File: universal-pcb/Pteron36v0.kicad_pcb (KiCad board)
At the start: 2 copper layers, 140.1 x 108.1 mm, 62 parts, among them J1 AudioJack4, J2 AudioJack4, J3 Conn_01x04, SW10 SW_PUSH, SW12 SW_PUSH, SW13 SW_PUSH, SW14 SW_PUSH, SW15 SW_PUSH, SW17 SW_PUSH, SW18 SW_PUSH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

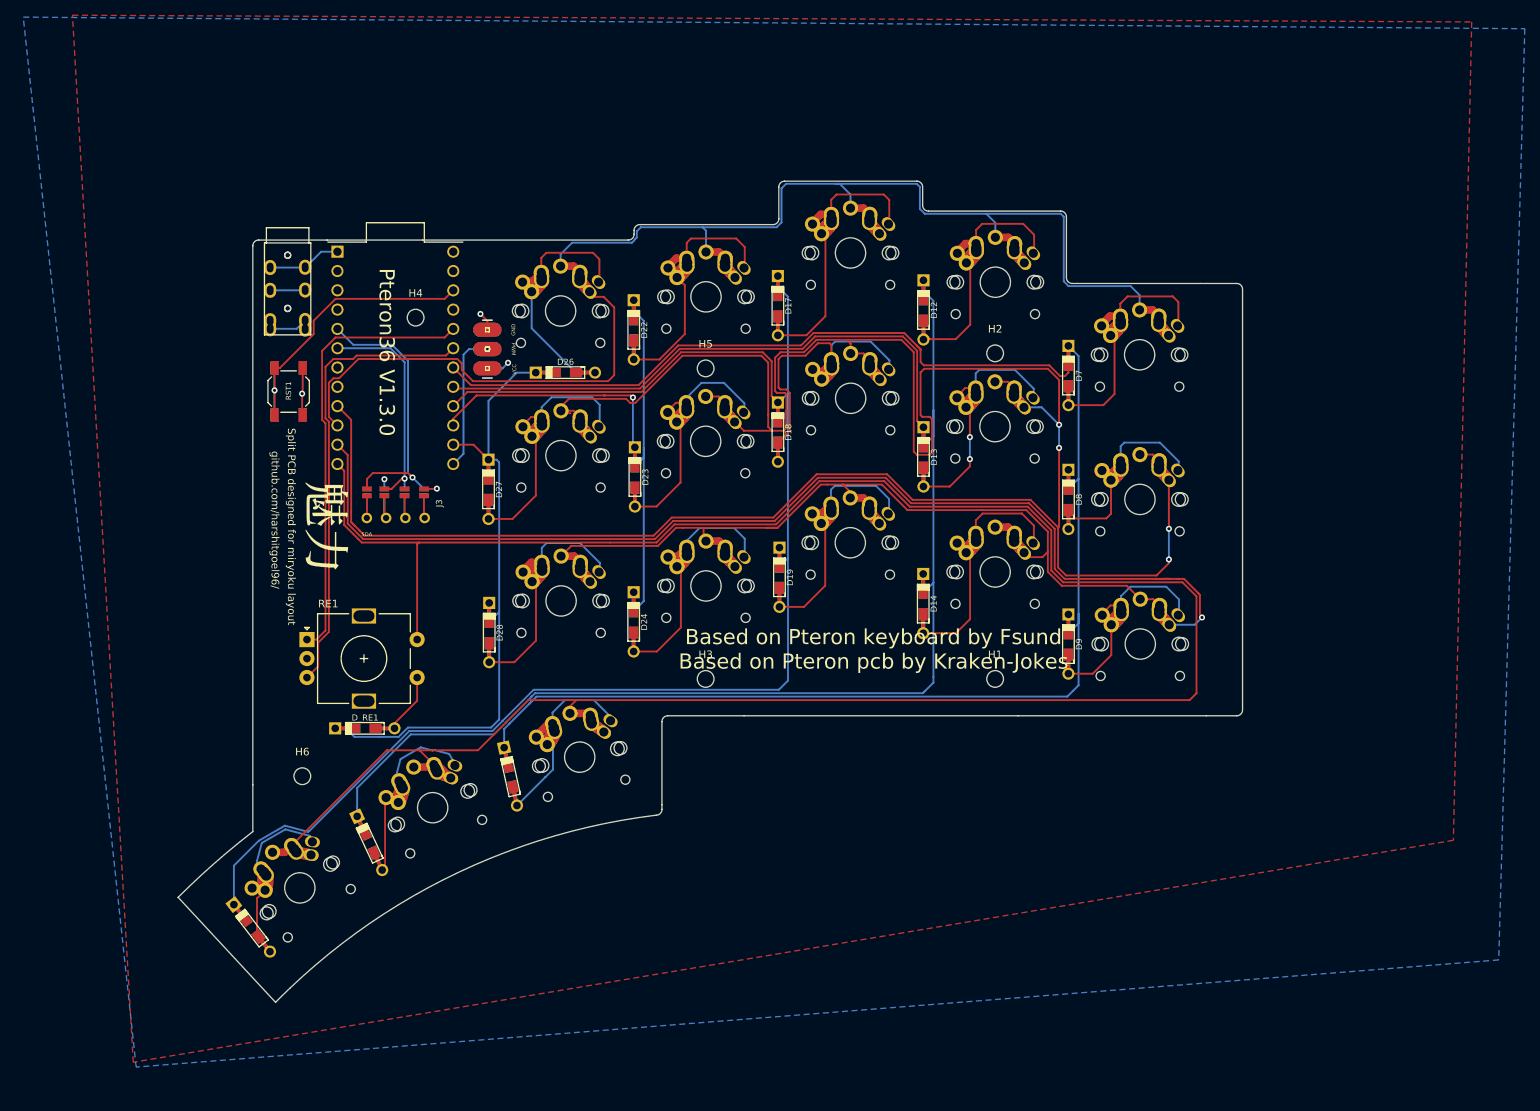
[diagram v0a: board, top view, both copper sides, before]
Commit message: update universal pcb with curvy layout
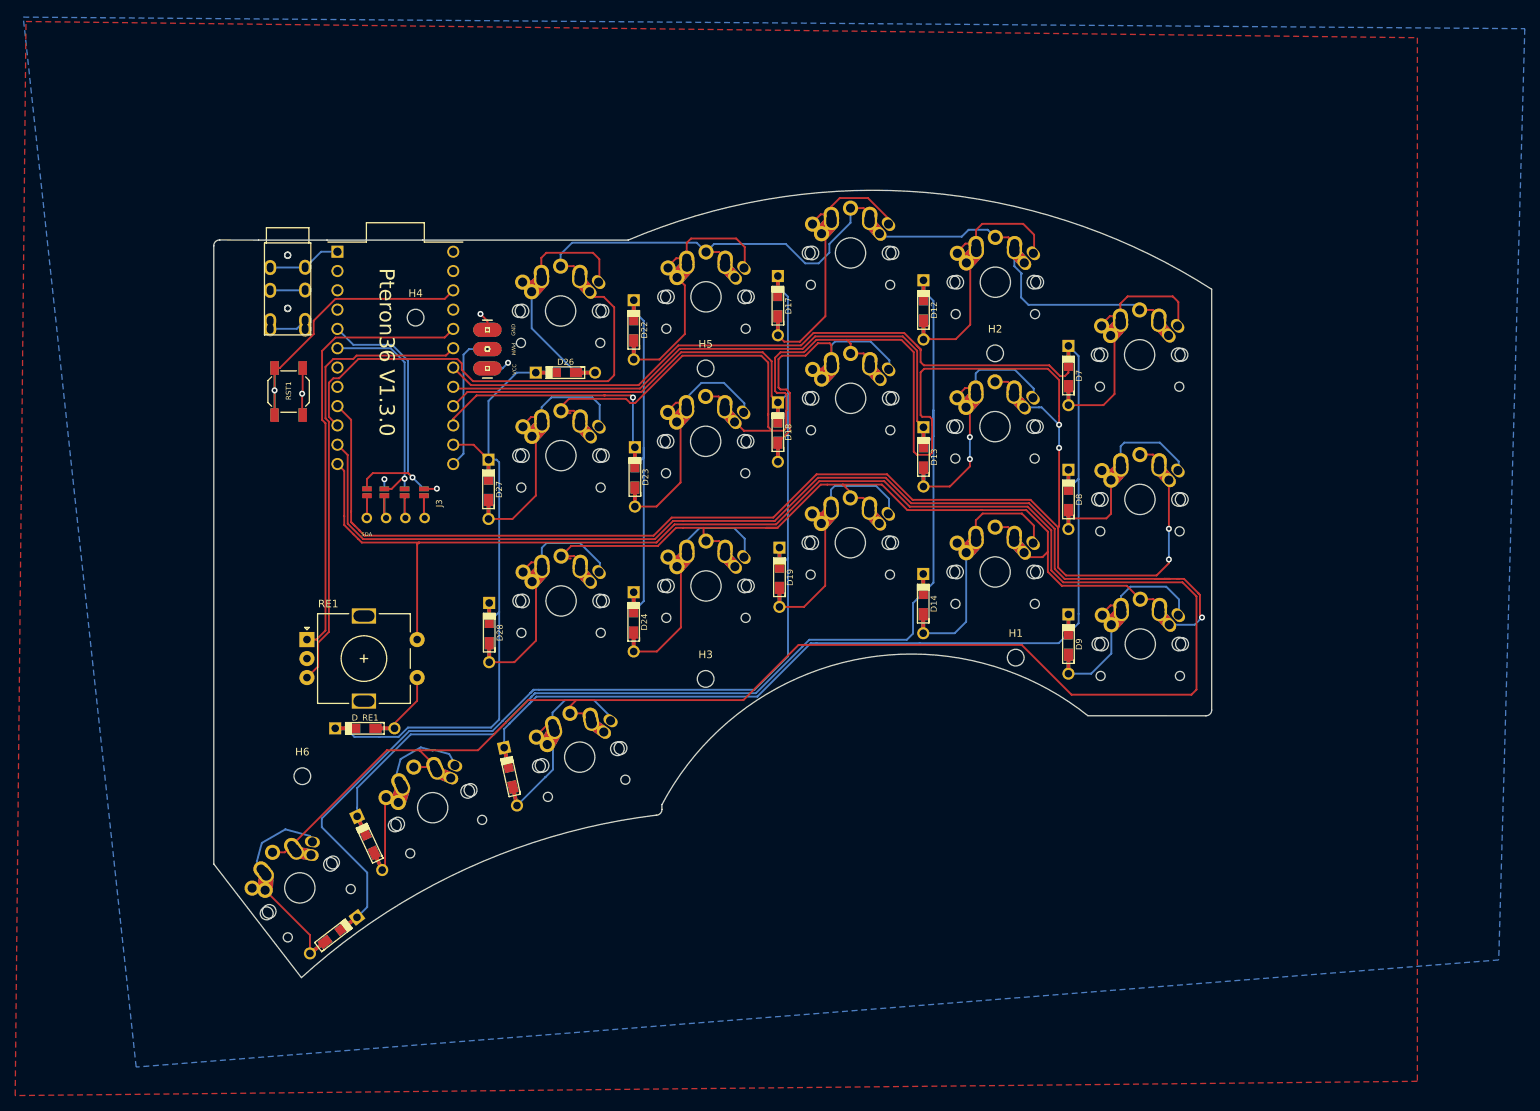
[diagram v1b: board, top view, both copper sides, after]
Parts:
- removed LOGO1, LOGO2: LOGO-OTL, personal-logo:miryoku-kicad-small
- moved D20 10.8 mm to (90.7, 140.1), turned to 37.5 degrees
- moved H1 3.90 mm to (180.5, 103.5)
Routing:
- net /Row1: track 202.0 -> 177.6 mm
- net /Col1: track 222.2 -> 214.3 mm
- net /Col2: track 220.2 -> 212.9 mm
- net /Row4: track 309.4 -> 314.6 mm
- net /Col3: track 196.5 -> 191.9 mm
- net Net-(D20-Pad2): track 24.2 -> 28.3 mm
- net Net-(D14-Pad2): track 35.0 -> 32.9 mm
- net Net-(D17-Pad2): track 39.3 -> 37.6 mm
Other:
- board size 140.1 x 108.1 mm -> 131.3 x 103.6 mm
- net class Default removed
- board text removed: "Based on Pteron keyboard by Fsund Based on Pteron pcb by Kraken-Jokes"
- board text removed: "Split PCB designed for miryoku layout"
- board text removed: "github.com/harshitgoel96/"
